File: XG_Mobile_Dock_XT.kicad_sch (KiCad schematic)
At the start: 45 parts, among them J1 5-1775443-8, J13 39301240, J14 I2C1, J2 20455-040E-76, J3 20455-040E-76, J5 USB_C_Receptacle, J6 455860005, J7 10147430-113T0LF, SW1 SW_Push

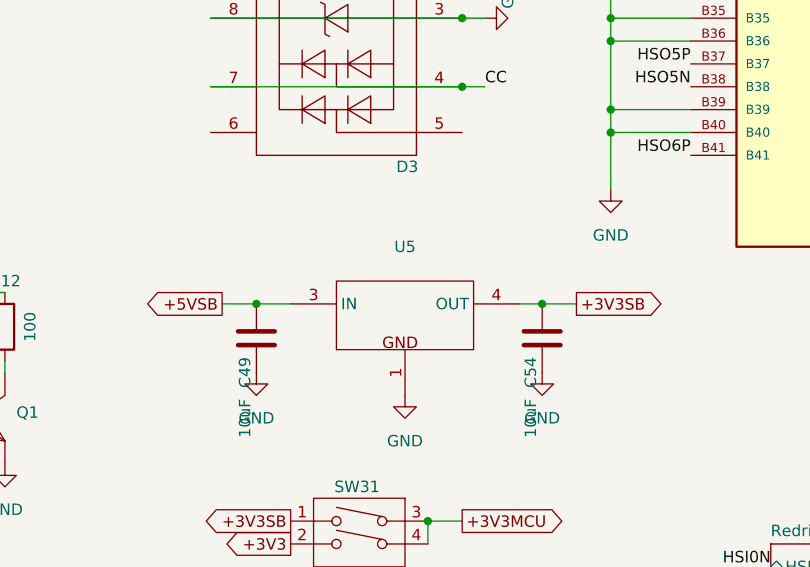
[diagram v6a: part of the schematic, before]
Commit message: adde better ldo
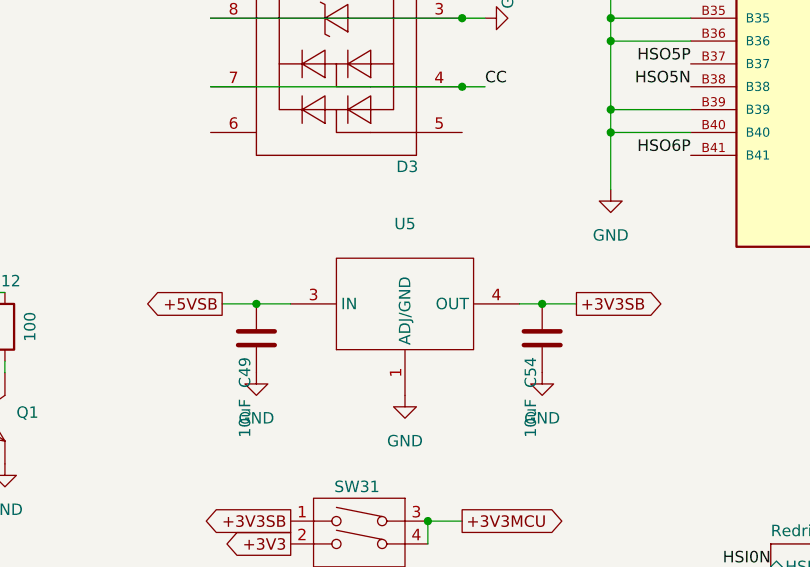
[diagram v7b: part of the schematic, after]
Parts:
- removed U5: ~, LD1086DT33TR:TO-252-2_L6.5-W6.1-P4.58-LS10.0-TL, symbol LD1086DT33TR:LD1086DT33TR
- added U5: ~, LD1085D2T33R:TO-263-2_L10.0-W9.1-P5.08-LS15.2-TL, symbol LD1085D2T33R:LD1085D2T33R
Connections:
- net +3V3SB: now also U5.4 (OUT)
- net +5VSB: now also U5.3 (IN)
- net GND: now also U5.1 (ADJ/GND)
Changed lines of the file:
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@@
-	)
-	(symbol
-		(lib_id "LD1086DT33TR:LD1086DT33TR")
-		(at 166.37 152.4 0)
-		(unit 1)
-		(exclude_from_sim no)
-		(in_bom yes)
-		(on_board yes)
-		(dnp no)
-		(fields_autoplaced yes)
-		(property "Reference" "U5"
-			(at 166.37 142.24 0)
-			(effects
-				(font
-					(size 1.27 1.27)
-				)
-			)
-		)
-		(property "Value" "~"
-			(at 166.37 144.78 0)
-			(effects
-				(font
-					(size 1.27 1.27)
-				)
-			)
-		)
-		(property "Footprint" "LD1086DT33TR:TO-252-2_L6.5-W6.1-P4.58-LS10.0-TL"
-			(at 166.37 152.4 0)
-			(effects
-				(font
-					(size 1.27 1.27)
-				)
-				(hide yes)
-			)
-		)
-		(property "Datasheet" "https://atta.szlcsc.com/upload/public/pdf/source/20170919/C12051_1505787088456976738.pdf"
-			(at 166.37 152.4 0)
-			(effects
-				(font
-					(size 1.27 1.27)
-				)
-				(hide yes)
-			)
-		)
-		(property "Description" "Output Type:Fixed Maximum Input Voltage:30V Output Voltage:3.3V Output Voltage:3.3V Output Current:1.5A Power Supply Rejection Ratio (PSRR):79dB@(120Hz) Dropout Voltage:1.5V@(1.5A) standby current:10mA Feature:Automotive Standard Certification；Thermal Pro"
-			(at 166.37 152.4 0)
-			(effects
-				(font
-					(size 1.27 1.27)
-				)
-				(hide yes)
-			)
-		)
-		(property "Manufacturer Part" "LD1086DT33TR"
-			(at 166.37 152.4 0)
-			(effects
-				(font
-					(size 1.27 1.27)
-				)
-				(hide yes)
-			)
-		)
-		(property "Manufacturer" "ST(意法半导体)"
-			(at 166.37 152.4 0)
-			(effects
-				(font
-					(size 1.27 1.27)
-				)
-				(hide yes)
-			)
-		)
-		(property "Supplier Part" "C12051"
-			(at 166.37 152.4 0)
-			(effects
-				(font
-					(size 1.27 1.27)
-				)
-				(hide yes)
-			)
-		)
-		(property "Supplier" "LCSC"
-			(at 166.37 152.4 0)
-			(effects
-				(font
-					(size 1.27 1.27)
-				)
-				(hide yes)
-			)
-		)
-		(property "LCSC Part Name" "1.5 A可调与固定低压降正电压稳压器"
-			(at 166.37 152.4 0)
-			(effects
-				(font
-					(size 1.27 1.27)
-				)
-				(hide yes)
-			)
-		)
-		(pin "4"
-		)
-		(pin "3"
-		)
-		(pin "1"
-		)
-		(instances
-			(project ""
-				(path "/f97e6956-ab08-42cb-8fed-03fa58e87f0e"
-					(reference "U5")
-					(unit 1)
-				)
-			)
-		)
 	)
 	(symbol
@@
 					(unit 1)
 				)
+			)
+		)
+	)
+	(symbol
+		(lib_id "LD1085D2T33R:LD1085D2T33R")
+		(at 166.37 151.13 0)
+		(unit 1)
+		(exclude_from_sim no)
+		(in_bom yes)
+		(on_board yes)
+		(dnp no)
+		(fields_autoplaced yes)
+		(property "Reference" "U5"
+			(at 166.37 139.7 0)
+			(effects
+				(font
+					(size 1.27 1.27)
+				)
+			)
+		)
+		(property "Value" "~"
+			(at 166.37 142.24 0)
+			(effects
+				(font
+					(size 1.27 1.27)
+				)
+			)
+		)
+		(property "Footprint" "LD1085D2T33R:TO-263-2_L10.0-W9.1-P5.08-LS15.2-TL"
+			(at 166.37 151.13 0)
+			(effects
+				(font
+					(size 1.27 1.27)
+				)
+				(hide yes)
+			)
+		)
+		(property "Datasheet" "https://item.szlcsc.com/datasheet/LD1085D2T33R/8390.html"
+			(at 166.37 151.13 0)
+			(effects
+				(font
+					(size 1.27 1.27)
+				)
+				(hide yes)
+			)
+		)
+		(property "Description" "Output Type:Fixed Voltage - Supply:30V Output Voltage:3.3V Output Voltage:3.3V Output Current:3A Power Supply Rejection Ratio (PSRR):72dB@(120Hz) Voltage Dropout:1.3V@(3A) standby current:5mA Noise:0.003%Vout Features:Over Temperature Protection Operating"
+			(at 166.37 151.13 0)
+			(effects
+				(font
+					(size 1.27 1.27)
+				)
+				(hide yes)
+			)
+		)
+		(property "Part_Number" "LD1085D2T33R"
+			(at 166.37 151.13 0)
+			(effects
+				(font
+					(size 1.27 1.27)
+				)
+				(hide yes)
+			)
+		)
+		(property "LCSC" "C7913"
+			(at 166.37 151.13 0)
+			(effects
+				(font
+					(size 1.27 1.27)
+				)
+				(hide yes)
+			)
+		)
+		(pin "4"
+		)
+		(pin "3"
+		)
+		(pin "1"
+		)
+		(instances
+			(project ""
+				(path "/f97e6956-ab08-42cb-8fed-03fa58e87f0e"
+					(reference "U5")
+					(unit 1)
+				)

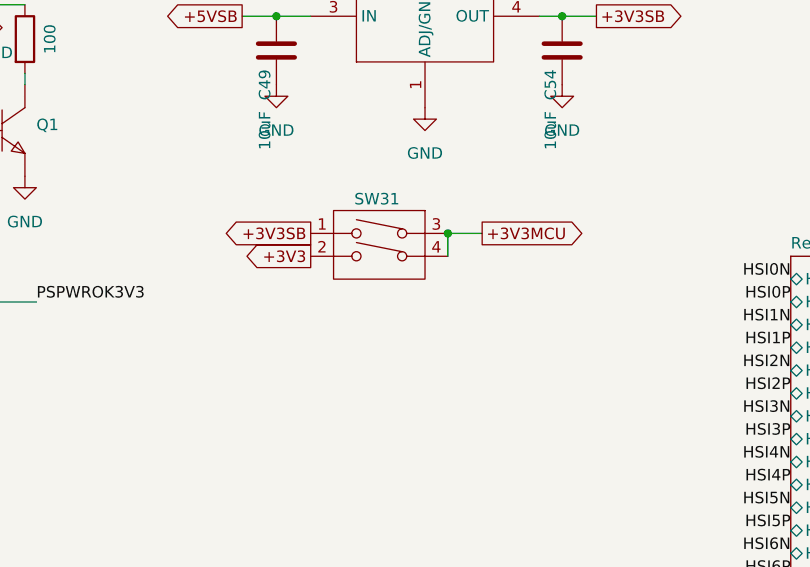
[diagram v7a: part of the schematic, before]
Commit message: added better switch for mcu power control
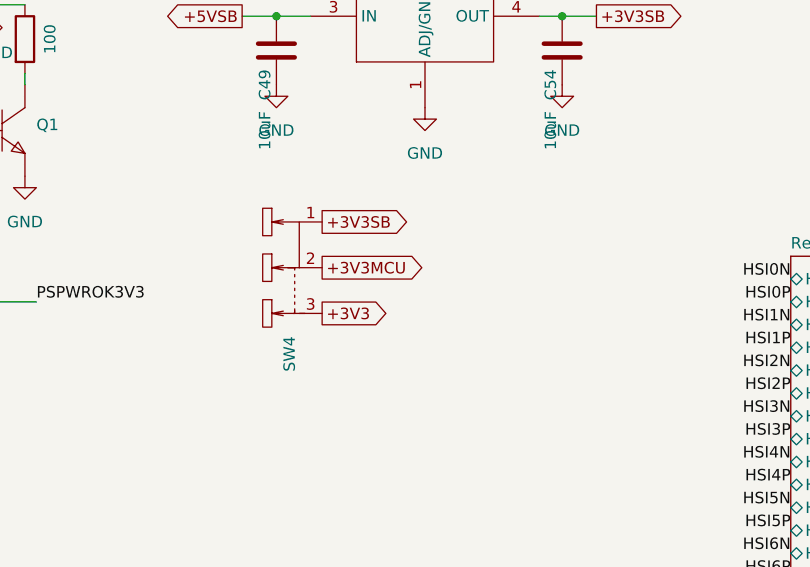
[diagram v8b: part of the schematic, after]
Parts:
- removed SW31: ~, DSWB02LHGET:SW-TH_DSWB02LHGET, symbol DSWB02LHGET:DSWB02LHGET
- added SW4: ~, SS-12D10L5:SW-TH_SS-12D10L5, symbol SS-12D10L5:SS-12D10L5
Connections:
- net +3V3: now also SW4.3
- net +3V3MCU: now also SW4.2
- net +3V3SB: now also SW4.1
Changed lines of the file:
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@@
 	)
 	(junction
-		(at 168.91 172.72)
-		(diameter 0)
-		(color 0 0 0 0)
-	)
-	(junction
 		(at 189.23 83.82)
 		(diameter 0)
@@
 	(wire
 		(pts
-			(xy 168.91 172.72) (xy 168.91 175.26)
-		)
-		(stroke
-			(width 0)
-			(type default)
-		)
-	)
-	(wire
-		(pts
 			(xy 236.22 88.9) (xy 236.22 96.52)
 		)
@@
 	(wire
 		(pts
-			(xy 168.91 172.72) (xy 172.72 172.72)
-		)
-		(stroke
-			(width 0)
-			(type default)
-		)
-	)
-	(wire
-		(pts
 			(xy 74.93 72.39) (xy 69.85 72.39)
 		)
@@
 	(global_label "+3V3"
 		(shape output)
-		(at 153.67 175.26 180)
+		(at 154.94 181.61 0)
 		(fields_autoplaced yes)
 		(effects
@@
 				(size 1.27 1.27)
 			)
-			(justify right)
+			(justify left)
 		)
 		(property "Intersheetrefs" "${INTERSHEET_REFS}"
-			(at 145.6048 175.26 0)
+			(at 163.0052 181.61 0)
 			(effects
 				(font
 					(size 1.27 1.27)
 				)
-				(justify right)
+				(justify left)
 				(hide yes)
 			)
@@
 	(global_label "+3V3SB"
 		(shape output)
-		(at 153.67 172.72 180)
+		(at 154.94 171.45 0)
 		(fields_autoplaced yes)
 		(effects
@@
 				(size 1.27 1.27)
 			)
-			(justify right)
+			(justify left)
 		)
 		(property "Intersheetrefs" "${INTERSHEET_REFS}"
-			(at 143.1253 172.72 0)
+			(at 165.4847 171.45 0)
 			(effects
 				(font
 					(size 1.27 1.27)
 				)
-				(justify right)
+				(justify left)
 				(hide yes)
 			)
@@
 	(global_label "+3V3MCU"
 		(shape output)
-		(at 172.72 172.72 0)
+		(at 154.94 176.53 0)
 		(fields_autoplaced yes)
 		(effects
@@
 		)
 		(property "Intersheetrefs" "${INTERSHEET_REFS}"
-			(at 184.8371 172.72 0)
+			(at 167.0571 176.53 0)
 			(effects
 				(font
@@
 	)
 	(symbol
+		(lib_id "SS-12D10L5:SS-12D10L5")
+		(at 152.4 176.53 270)
+		(unit 1)
+		(exclude_from_sim no)
+		(in_bom yes)
+		(on_board yes)
+		(dnp no)
+		(fields_autoplaced yes)
+		(property "Reference" "SW4"
+			(at 151.3206 184.15 0)
+			(effects
+				(font
+					(size 1.27 1.27)
+				)
+				(justify left)
+			)
+		)
+		(property "Value" "~"
+			(at 149.4155 184.15 0)
+			(effects
+				(font
+					(size 1.27 1.27)
+				)
+				(justify left)
+			)
+		)
+		(property "Footprint" "SS-12D10L5:SW-TH_SS-12D10L5"
+			(at 152.4 176.53 0)
+			(effects
+				(font
+					(size 1.27 1.27)
+				)
+				(hide yes)
+			)
+		)
+		(property "Datasheet" "https://item.szlcsc.com/datasheet/SS-12D10L5/300104.html"
+			(at 152.4 176.53 0)
+			(effects
+				(font
+					(size 1.27 1.27)
+				)
+				(hide yes)
+			)
+		)
+		(property "Description" "Circuit:SPDT Actuator Style:Rectangular Columnar Termination Style:PC Pin Length:13mm Width:6.8mm Switch Height:6.4mm Mounting Type:Through Hole Actuator Color:Black Current Rating:3A Voltage Rating:125V Life:10,000 Cycles Operating Temperature:-40°C~+85°C"
+			(at 152.4 176.53 0)
+			(effects
+				(font
+					(size 1.27 1.27)
+				)
+				(hide yes)
+			)
+		)
+		(property "Part_Number" "SS-12D10L5"
+			(at 152.4 176.53 0)
+			(effects
+				(font
+					(size 1.27 1.27)
+				)
+				(hide yes)
+			)
+		)
+		(property "Manufacturer" "XKB Connection(中国星坤)"
+			(at 152.4 176.53 0)
+			(effects
+				(font
+					(size 1.27 1.27)
+				)
+				(hide yes)
+			)
+		)
+		(property "LCSC" "C319012"
+			(at 152.4 176.53 0)
+			(effects
+				(font
+					(size 1.27 1.27)
+				)
+				(hide yes)
+			)
+		)
+		(pin "3"
+		)
+		(pin "1"
+		)
+		(pin "2"
+		)
+		(instances
+			(project ""
+				(path "/f97e6956-ab08-42cb-8fed-03fa58e87f0e"
+					(reference "SW4")
+					(unit 1)
+				)
+			)
+		)
+	)
+	(symbol
 		(lib_id "1-1775099-3:1-1775099-3")
 		(at 69.85 148.59 0)
@@
 					(unit 1)
 				)
-			)
-		)
-	)
-	(symbol
-		(lib_id "DSWB02LHGET:DSWB02LHGET")
-		(at 161.29 173.99 90)
-		(mirror x)
-		(unit 1)
-		(exclude_from_sim no)
-		(in_bom yes)
-		(on_board yes)
-		(dnp no)
-		(property "Reference" "SW31"
-			(at 161.036 168.91 90)
-			(effects
-				(font
-					(size 1.27 1.27)
-				)
-			)
-		)
-		(property "Value" "~"
-			(at 161.29 168.91 90)
-			(effects
-				(font
-					(size 1.27 1.27)
-				)
-			)
-		)
-		(property "Footprint" "DSWB02LHGET:SW-TH_DSWB02LHGET"
-			(at 161.29 173.99 0)
-			(effects
-				(font
-					(size 1.27 1.27)
-				)
-				(hide yes)
-			)
-		)
-		(property "Datasheet" "https://atta.szlcsc.com/upload/public/pdf/source/20230906/EFD9230F686161BBBCD1B62855702D44.pdf"
-			(at 161.29 173.99 0)
-			(effects
-				(font
-					(size 1.27 1.27)
-				)
-				(hide yes)
-			)
-		)
-		(property "Description" "Type:平拨,凸起式 Circuit:SPST Number of Positions:2Bit Lead Pitch:2.54mm Operating Life:- Color:Red"
-			(at 161.29 173.99 0)
-			(effects
-				(font
-					(size 1.27 1.27)
-				)
-				(hide yes)
-			)
-		)
-		(property "Part_Number" "DSWB02LHGET"
-			(at 161.29 173.99 0)
-			(effects
-				(font
-					(size 1.27 1.27)
-				)
-				(hide yes)
-			)
-		)
-		(property "Manufacturer" "YE"
-			(at 161.29 173.99 0)
-			(effects
-				(font
-					(size 1.27 1.27)
-				)
-				(hide yes)
-			)
-		)
-		(property "LCSC" "C99421"
-			(at 161.29 173.99 0)
-			(effects
-				(font
-					(size 1.27 1.27)
-				)
-				(hide yes)
-			)
-		)
-		(pin "4"
-		)
-		(pin "3"
-		)
-		(pin "1"
-		)
-		(pin "2"
-		)
-		(instances
-			(project "XG_Mobile_Dock_XT"
-				(path "/f97e6956-ab08-42cb-8fed-03fa58e87f0e"
-					(reference "SW31")
-					(unit 1)
-				)
